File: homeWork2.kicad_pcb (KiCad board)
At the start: 2 copper layers, 125 x 99.9 mm, 48 parts, among them J1 Barrel_Jack_Switch_SMT, U1 LM7805_TO220

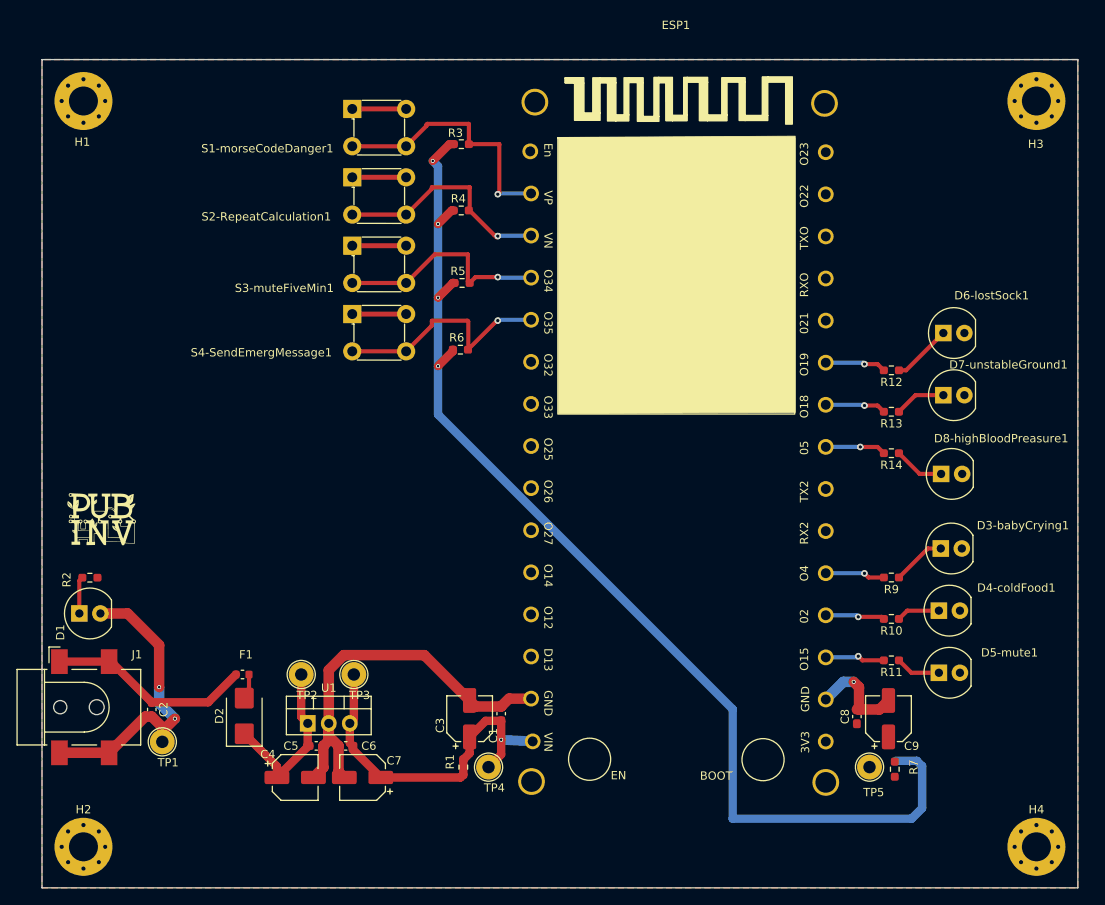
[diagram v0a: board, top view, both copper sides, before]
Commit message: changing net names to better use the net classes. Corrected a short across resistor R1.
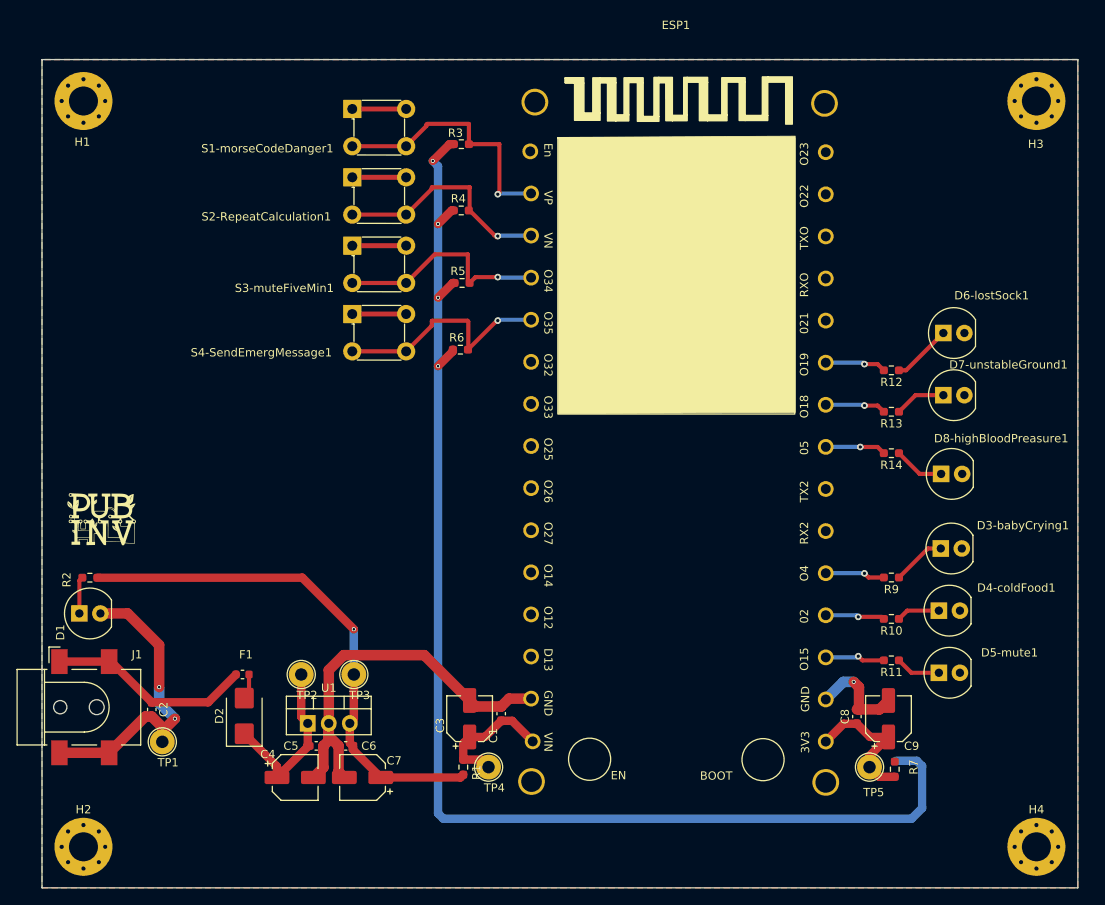
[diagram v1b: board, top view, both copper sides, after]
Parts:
- turned R1 to -90 degrees
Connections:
- net Net-(ESP1-3V3) renamed /+3V3esp32
- C1 pad 1: +5V -> /+5Vesp32
- C3 pad 1: +5V -> /+5Vesp32
- ESP1 pad 1: +5V -> /+5Vesp32
- R1 pad 1: +5V -> /+5Vesp32
- TP4 pad 1: +5V -> /+5Vesp32
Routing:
- net +3.3V: track 137.7 -> 158.1 mm
- net +5V: track 43.8 -> 63.3 mm
- net /+3V3esp32: track 0.00 -> 17.2 mm
- net /+5Vesp32: track 0.00 -> 15.9 mm

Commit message: Rerouting +3v3 to the pull up resistors from the bottom layer to the top layer.
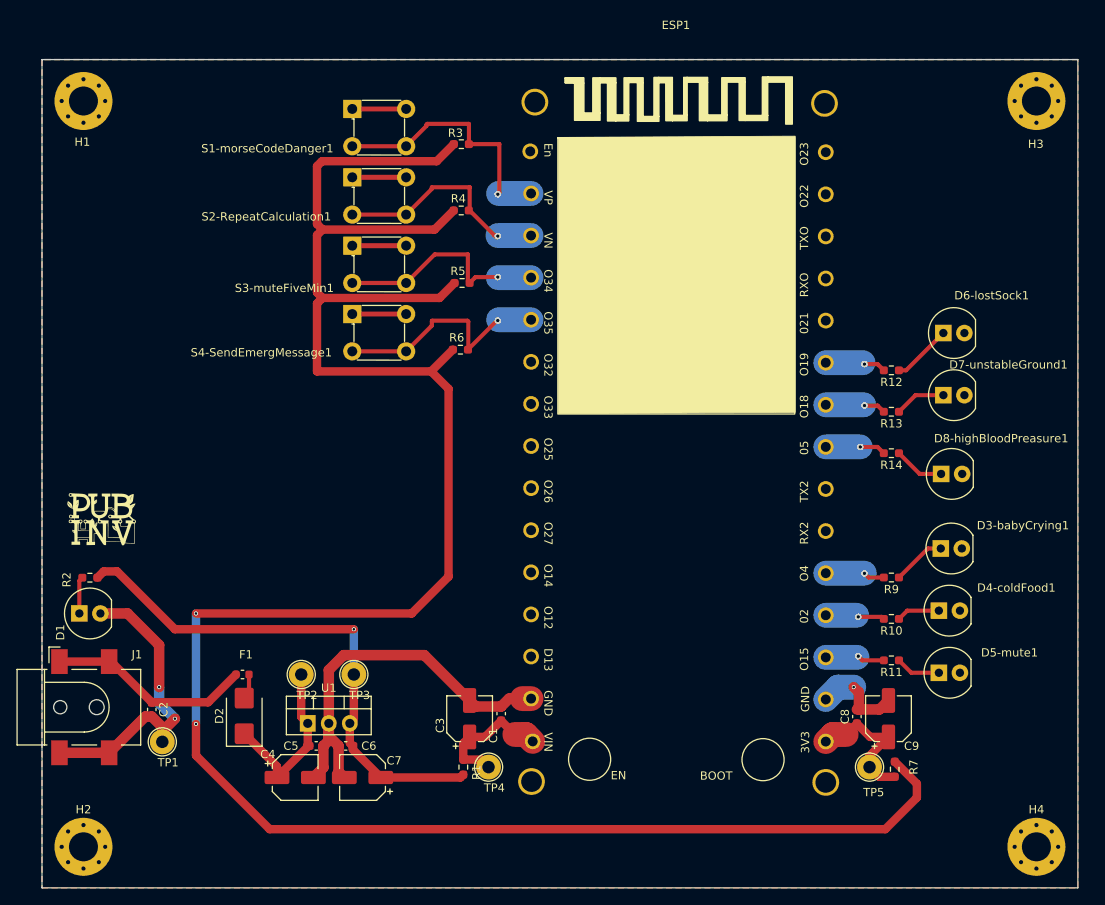
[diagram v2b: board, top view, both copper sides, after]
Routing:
- net +3.3V: track 158.1 -> 267.2 mm, vias 4 -> 2
- net GND: track 125.6 -> 124.7 mm
- net +5V: track 63.3 -> 63.9 mm

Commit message: Edited the ESP32 footprint. Rerouted the PCBa and added female socket connectors to the ESP32 and two others to connect an LCD and a DFPLAYER
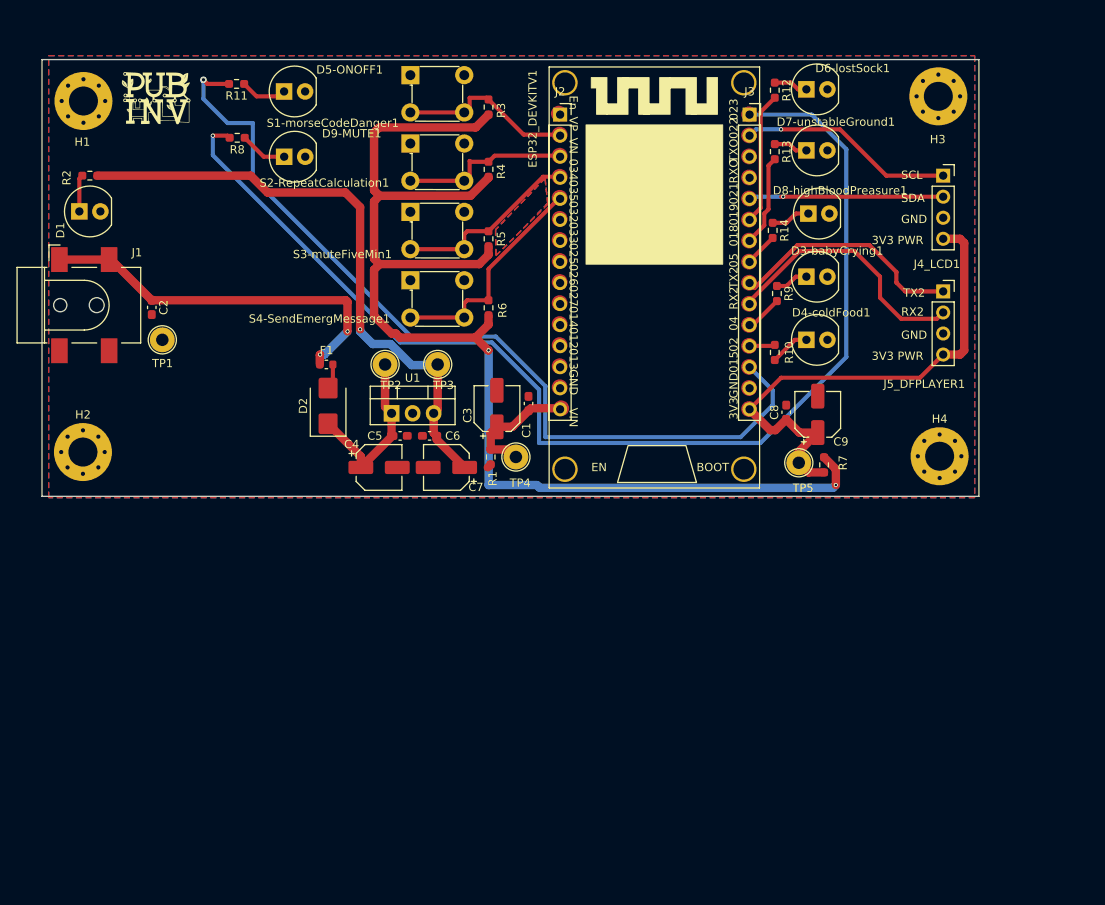
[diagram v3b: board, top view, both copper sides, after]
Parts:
- added D9-MUTE1: LED_T1.75_CLEAR_RED, PubInv_KiCad_PCB:LED_5mm_Radial, F.Cu at (81.8, 61.7)
- added J2: Conn_01x15_Socket, Connector_PinSocket_2.54mm:PinSocket_1x15_P2.54mm_Vertical, F.Cu at (112.5, 56.6)
- added J3: Conn_01x15_Socket, Connector_PinSocket_2.54mm:PinSocket_1x15_P2.54mm_Vertical, F.Cu at (135.4, 56.6)
- added J4_LCD1: Conn_01x04_Socket_LCD, Connector_PinSocket_2.54mm:PinSocket_1x04_P2.54mm_Vertical, F.Cu at (158.8, 64.0)
- added J5_DFPLAYER1: Conn_01x04_Socket_DFPLAYER, Connector_PinSocket_2.54mm:PinSocket_1x04_P2.54mm_Vertical, F.Cu at (158.8, 78.0)
- added R8: 60 ohm, Resistor_SMD:R_0603_1608Metric_Pad0.98x0.95mm_HandSolder, F.Cu at (73.6, 59.4)
- ESP32_DEVKITV1: renamed from ESP1; footprint esp32 15 pin Library:esp32 -> PubInv_KiCad_PCB:ESP32_DEVKITV1
- moved D5-ONOFF1 105.7 mm to (81.8, 53.8)
- moved R11 105.3 mm to (73.5, 52.9)
- moved G*** 51.2 mm to (63.8, 54.9)
- moved H4 48.6 mm to (158.3, 97.9)
- moved D1 48.5 mm to (57.0, 68.3)
- moved J1 48.5 mm to (55.1, 79.6)
- moved R2 48.5 mm to (55.8, 64.0)
- moved TP1 48.5 mm to (64.5, 83.8)
- moved C2 48.5 mm to (63.2, 79.9)
- moved H2 47.6 mm to (54.9, 97.4)
- moved C5 38.8 mm to (93.2, 95.4)
- moved C6 38.8 mm to (96.8, 95.4)
- moved F1 38.8 mm to (84.3, 86.8)
- moved TP2 38.8 mm to (91.4, 86.8)
- moved TP3 38.8 mm to (97.7, 86.8)
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- renumbered D5-mute1 to D5-ONOFF1
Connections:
- ESP32_DEVKITV1 pad 10: unconnected-(ESP1-O32-Pad10) -> Net-(ESP32_DEVKITV1-GPIO32)
- ESP32_DEVKITV1 pad 15: unconnected-(ESP1-En-Pad15) -> Net-(ESP32_DEVKITV1-En)
- ESP32_DEVKITV1 pad 16: unconnected-(ESP1-O23-Pad16) -> Net-(ESP32_DEVKITV1-GPIO23)
- ESP32_DEVKITV1 pad 17: unconnected-(ESP1-O22-Pad17) -> Net-(ESP32_DEVKITV1-GPIO22_SCL)
- ESP32_DEVKITV1 pad 18: unconnected-(ESP1-TX0-Pad18) -> Net-(ESP32_DEVKITV1-GPIO1_TX0)
- ESP32_DEVKITV1 pad 19: unconnected-(ESP1-RX0-Pad19) -> Net-(ESP32_DEVKITV1-GPIO_RX0)
- ESP32_DEVKITV1 pad 20: unconnected-(ESP1-O21-Pad20) -> Net-(ESP32_DEVKITV1-GPIO21_SDA)
- ESP32_DEVKITV1 pad 24: unconnected-(ESP1-TX2-Pad24) -> Net-(ESP32_DEVKITV1-GPIO17_TX2)
- ESP32_DEVKITV1 pad 25: unconnected-(ESP1-RX2-Pad25) -> Net-(ESP32_DEVKITV1-GPIO16_RX2)
- ESP32_DEVKITV1 pad 3: unconnected-(ESP1-O13-Pad3) -> Net-(ESP32_DEVKITV1-GPIO13)
- ESP32_DEVKITV1 pad 4: unconnected-(ESP1-O12-Pad4) -> Net-(ESP32_DEVKITV1-GPIO12)
- ESP32_DEVKITV1 pad 5: unconnected-(ESP1-O1-Pad5) -> Net-(ESP32_DEVKITV1-GPIO1)
- ESP32_DEVKITV1 pad 6: unconnected-(ESP1-O27-Pad6) -> Net-(ESP32_DEVKITV1-GPIO27)
- ESP32_DEVKITV1 pad 7: unconnected-(ESP1-O26-Pad7) -> Net-(ESP32_DEVKITV1-GPIO26)
- ESP32_DEVKITV1 pad 8: unconnected-(ESP1-O25-Pad8) -> Net-(ESP32_DEVKITV1-GPIO25)
- ESP32_DEVKITV1 pad 9: unconnected-(ESP1-O33-Pad9) -> Net-(ESP32_DEVKITV1-GPIO33)
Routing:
- net Net-(ESP32_DEVKITV1-GPIO23): track 0.00 -> 141.9 mm, vias 0 -> 1
- net GND: track 124.7 -> 0.00 mm, vias 3 -> 0
- net +3.3V: track 267.2 -> 147.6 mm
- net Net-(ESP32_DEVKITV1-GPIO15): track 7.27 -> 106.2 mm
- net /+3V3esp32: track 17.2 -> 63.2 mm
- net Net-(ESP32_DEVKITV1-GPIO16_RX2): track 0.00 -> 31.4 mm
- net Net-(ESP32_DEVKITV1-GPIO17_TX2): track 0.00 -> 28.8 mm
- net Net-(ESP32_DEVKITV1-GPIO22_SCL): track 0.00 -> 26.0 mm, vias 0 -> 1
- net Net-(ESP32_DEVKITV1-GPIO21_SDA): track 0.00 -> 23.7 mm, vias 0 -> 1
- net /PVRAW: track 24.7 -> 46.1 mm, vias 0 -> 2
- net Net-(ESP32_DEVKITV1-VP_GPIO36): track 31.6 -> 21.2 mm, vias 1 -> 0
- net +5V: track 63.9 -> 74.0 mm
- net Net-(ESP32_DEVKITV1-GPIO19): track 7.39 -> 16.0 mm, vias 1 -> 0
- net Net-(ESP32_DEVKITV1-VN_GPIO39): track 27.6 -> 20.4 mm, vias 1 -> 0
- net Net-(D9-MUTE1-Pad1): track 0.00 -> 5.70 mm
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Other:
- board size 125 x 99.9 mm -> 113.1 x 52.7 mm
- board text added: "3V3 PWR"
- board text added: "GND"
- board text added: "RX2"
- board text added: "SCL"
- board text added: "SDA"
- board text added: "TX2"

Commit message: PCB and schematics edits. Added a connector for the UART interface and a connection for the I2C interface.
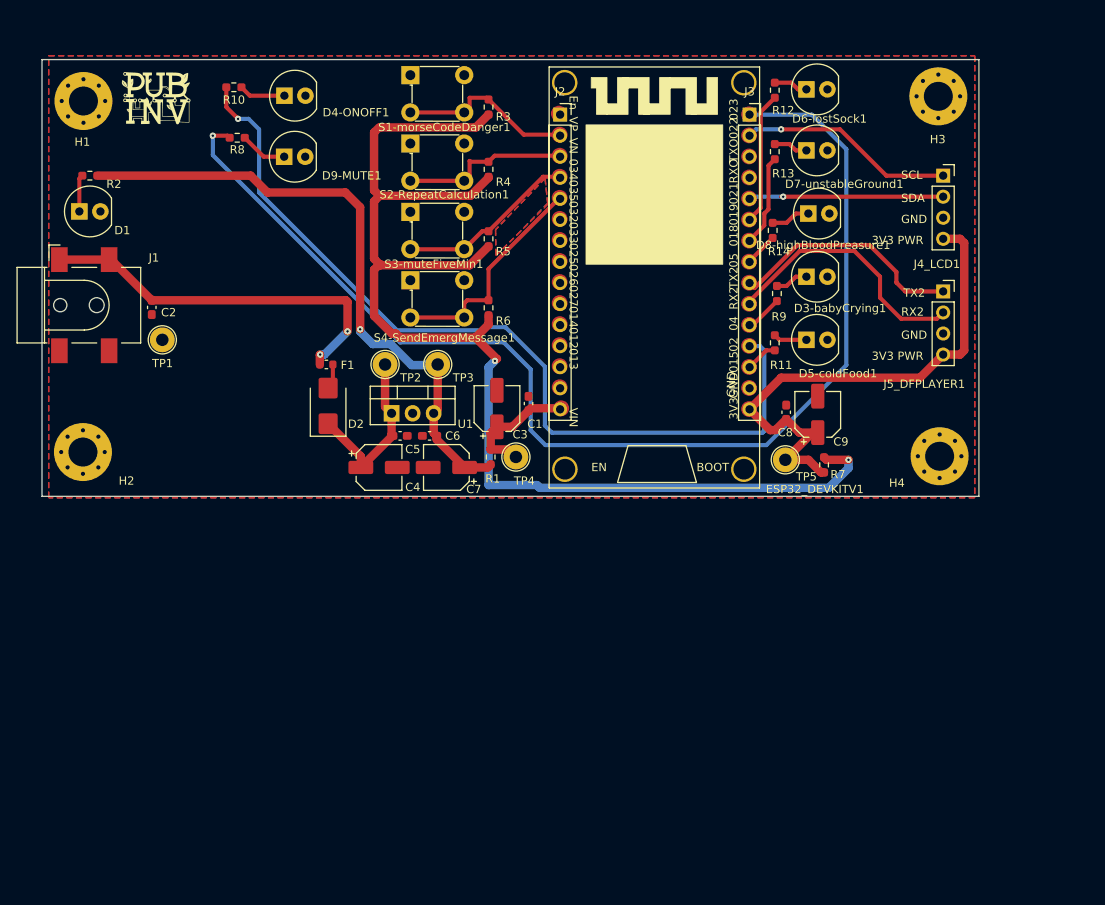
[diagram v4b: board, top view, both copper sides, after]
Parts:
- moved R10 72.7 mm to (73.2, 53.3), turned to 180 degrees
- moved R11 72.1 mm to (138.4, 84.2), turned to -90 degrees
- moved D5-coldFood1 69.8 mm to (144.8, 83.8)
- moved D4-ONOFF1 69.5 mm to (81.8, 54.4)
- moved TP5 1.67 mm to (139.7, 98.3)
- renumbered D4-coldFood1 to D4-ONOFF1, D5-ONOFF1 to D5-coldFood1
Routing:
- net Net-(ESP32_DEVKITV1-GPIO15): track 106.2 -> 3.89 mm, vias 1 -> 0
- net Net-(ESP32_DEVKITV1-GPIO2): track 3.15 -> 104.3 mm, vias 0 -> 1
- net +5V: track 74.0 -> 76.8 mm
- net +3.3V: track 147.6 -> 150.2 mm
- net /+3V3esp32: track 63.2 -> 65.7 mm
- net Net-(D5-coldFood1-Pad1): track 5.44 -> 4.04 mm
- net Net-(ESP32_DEVKITV1-GPIO23): track 141.9 -> 143.2 mm
- net Net-(ESP32_DEVKITV1-GPIO34): track 22.7 -> 21.7 mm
- net Net-(D4-ONOFF1-Pad1): track 4.82 -> 5.60 mm

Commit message: Cleared the ERC errors.
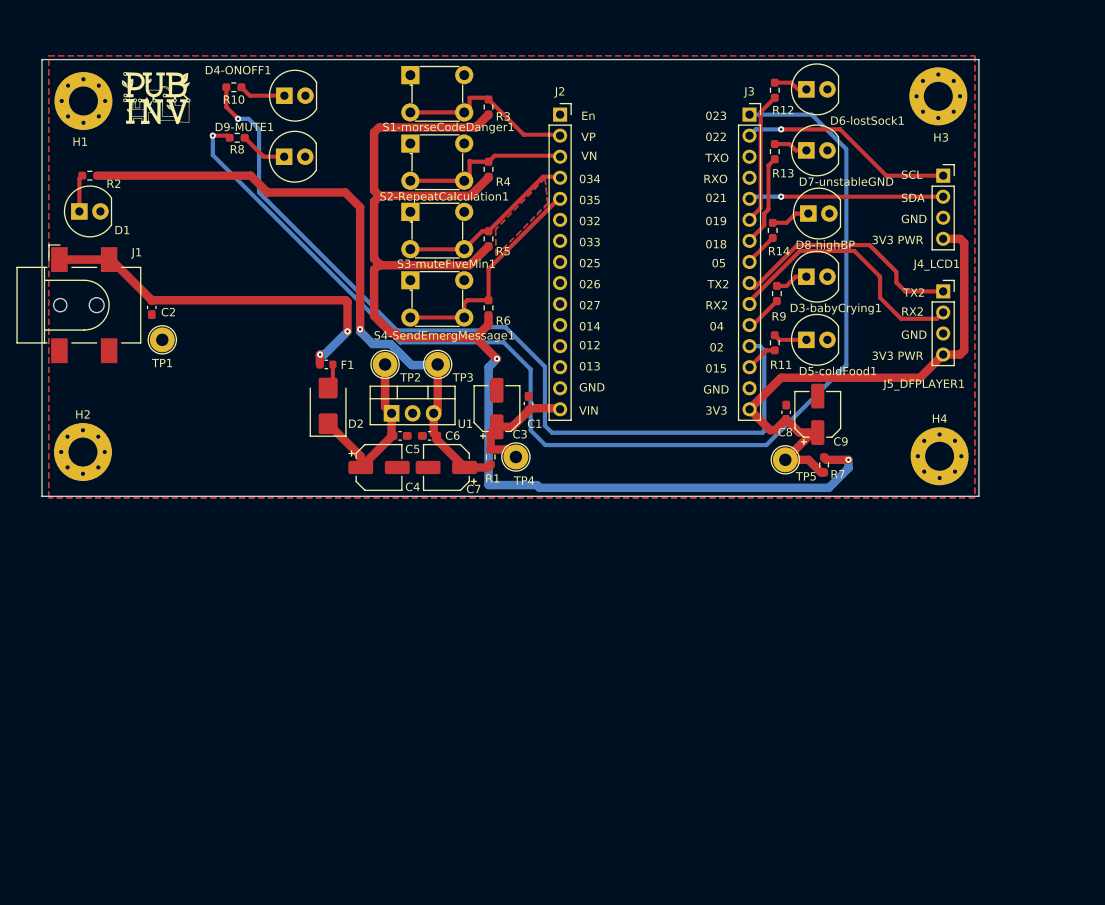
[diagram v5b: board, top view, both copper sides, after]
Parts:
- removed ESP32_DEVKITV1: ~, PubInv_KiCad_PCB:ESP32_DEVKITV1
- added ?: , clipboard:70bdaf9e-728c-4c59-bf8e-af8f097ba873, F.Cu at (115.3, 84.6)
- added ?: , clipboard:4d4f84bf-47b5-4440-bb6d-76d1ab99c339, F.Cu at (132.3, 57.7)
- added ?: , clipboard:061db143-2db6-424e-a8f9-62dfbcc2d95b, F.Cu at (132.3, 88.6)
- D3-babyCrying1, D4-ONOFF1, D5-coldFood1, D6-lostSock1, D9-MUTE1: footprint PubInv_KiCad_PCB:LED_5mm_Radial -> GeneralPurposeAlarmDevicePCB:LED_5mm_Radial
- D7-unstableGND: renamed from D7-unstableGround1; footprint PubInv_KiCad_PCB:LED_5mm_Radial -> GeneralPurposeAlarmDevicePCB:LED_5mm_Radial
- D8-highBP: renamed from D8-highBloodPreasure1; footprint PubInv_KiCad_PCB:LED_5mm_Radial -> GeneralPurposeAlarmDevicePCB:LED_5mm_Radial
- H1, H2, H3, H4: footprint PubInv_KiCad_PCB:MountingHole_3.5mm_Pad_Via -> GeneralPurposeAlarmDevicePCB:MountingHole_3.5mm_Pad_Via
- J1: footprint PubInv_KiCad_PCB:BarrelJack_CLIFF_FC681465S_SMT_Horizontal -> GeneralPurposeAlarmDevicePCB:BarrelJack_CLIFF_FC681465S_SMT_Horizontal
- S1-morseCodeDanger1, S2-RepeatCalculation1, S3-muteFiveMin1, S4-SendEmergMessage1: footprint PubInv_KiCad_PCB:Switch_Tactile_THT_6x6mm -> GeneralPurposeAlarmDevicePCB:Switch_Tactile_THT_6x6mm

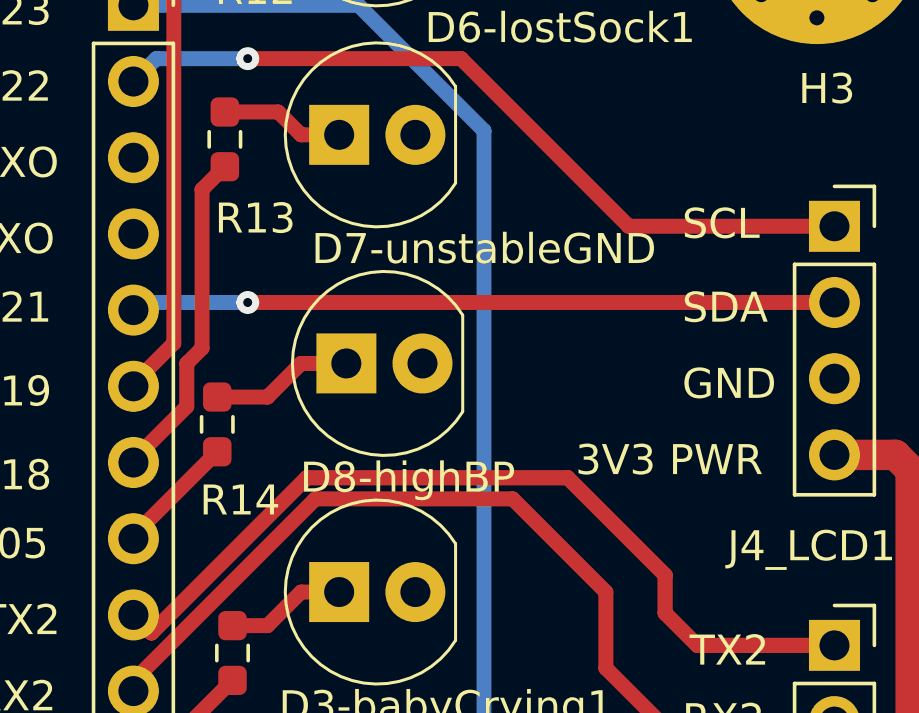
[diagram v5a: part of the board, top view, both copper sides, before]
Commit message: Cleared the DRC ERRORS.
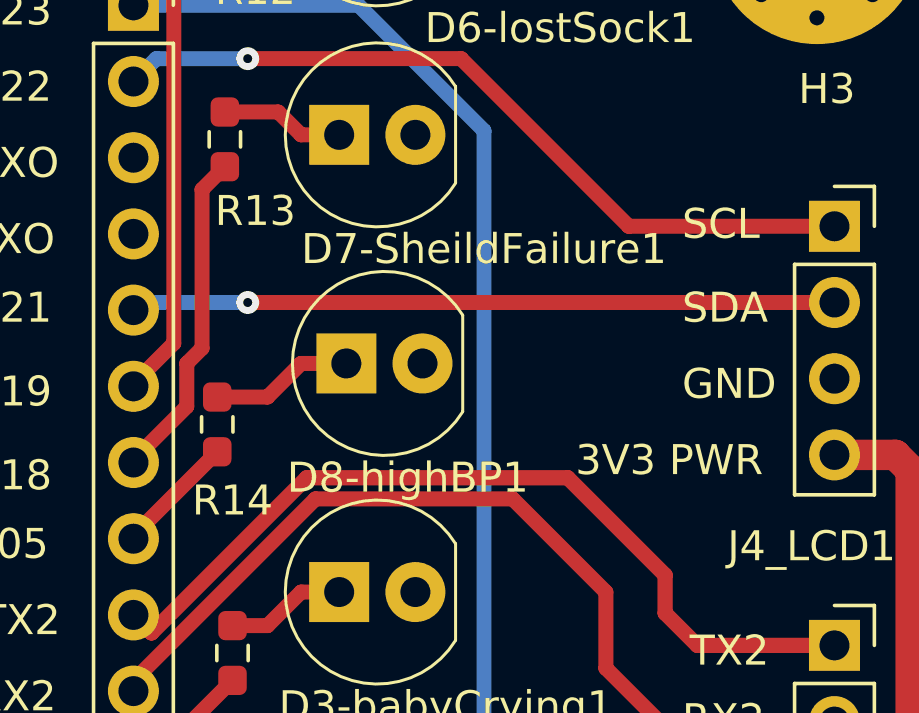
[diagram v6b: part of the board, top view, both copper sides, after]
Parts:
- added ?: , clipboard:4d4f84bf-47b5-4440-bb6d-76d1ab99c339, B.Cu at (130.6, 57.7)
- added ?: , clipboard:061db143-2db6-424e-a8f9-62dfbcc2d95b, B.Cu at (130.6, 88.6)
- added ?: , clipboard:70bdaf9e-728c-4c59-bf8e-af8f097ba873, B.Cu at (118.4, 84.6)
- added G***: LOGO, PubInv_KiCad_PCB:Logo_PI_BandW_70percent_10x10, B.Cu at (63.5, 54.9)
- renumbered D7-unstableGND to D7-SheildFailure1, D8-highBP to D8-highBP1
